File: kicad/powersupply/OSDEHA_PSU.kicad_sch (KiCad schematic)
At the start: 2 parts, among them J1 PSU HV, T1 Transformer_1P_2S

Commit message: up
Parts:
- removed T1: Transformer_1P_2S, symbol Device:Transformer_1P_2S
- added J3: AC secondaries, symbol Connector:Conn_01x06_Socket
- added R10: 976k, Resistor_THT:R_Axial_DIN0207_L6.3mm_D2.5mm_P10.16mm_Horizontal, symbol Device:R
- added R4, R9: 787k, Resistor_THT:R_Axial_DIN0207_L6.3mm_D2.5mm_P10.16mm_Horizontal, symbol Device:R
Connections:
- net HV_STABI1/AC1: now also J3.1 (Pin_1)
- net HV_STABI1/AC2: now also J3.2 (Pin_2)
- net HV_STABI2/AC1: now also J3.3 (Pin_3)
- net HV_STABI2/AC2: now also J3.4 (Pin_4)
- net HV_STABI3/DC-: now reaches J1.3 (Pin_3)
- new net HV_STABI1/RSET+: R4.2
- new net HV_STABI1/RSET-: R4.1
- new net HV_STABI2/RSET+: R9.2
- new net HV_STABI2/RSET-: R9.1
- new net HV_STABI3/AC1: J3.5 (Pin_5)
- new net HV_STABI3/AC2: J3.6 (Pin_6)
- new net HV_STABI3/RSET+: R10.2
- new net HV_STABI3/RSET-: R10.1
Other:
- added sheet HV_STABI3 (hv_stabi.kicad_sch)
- sheet HV_STABI1 ports: added RSET+, RSET-; removed none
- sheet HV_STABI2 ports: added RSET+, RSET-; removed none
- note added: "+440 V"
- note added: "-440 V"
- note added: "-550 V"
- note removed: "GRID BIAS"
- moved on the sheet: J1

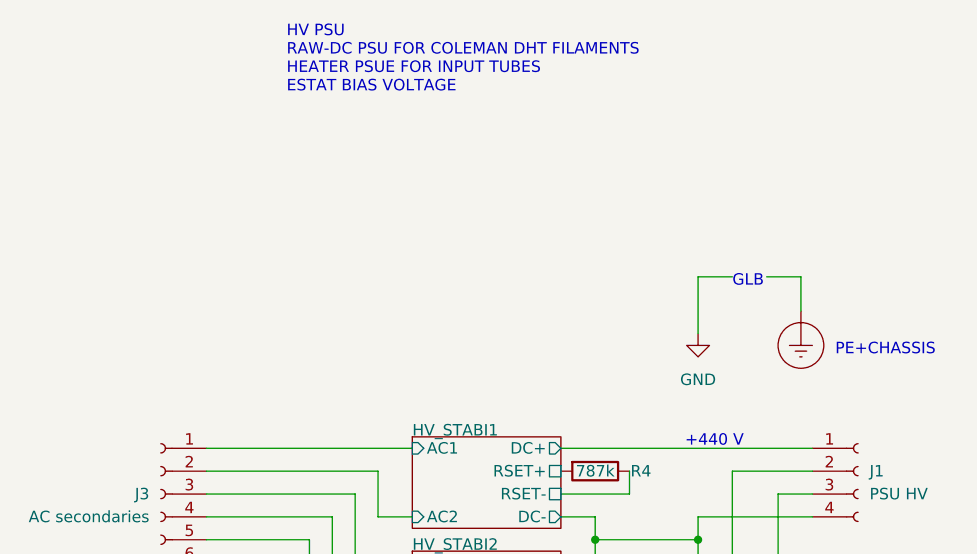
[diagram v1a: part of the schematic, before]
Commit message: add GLB
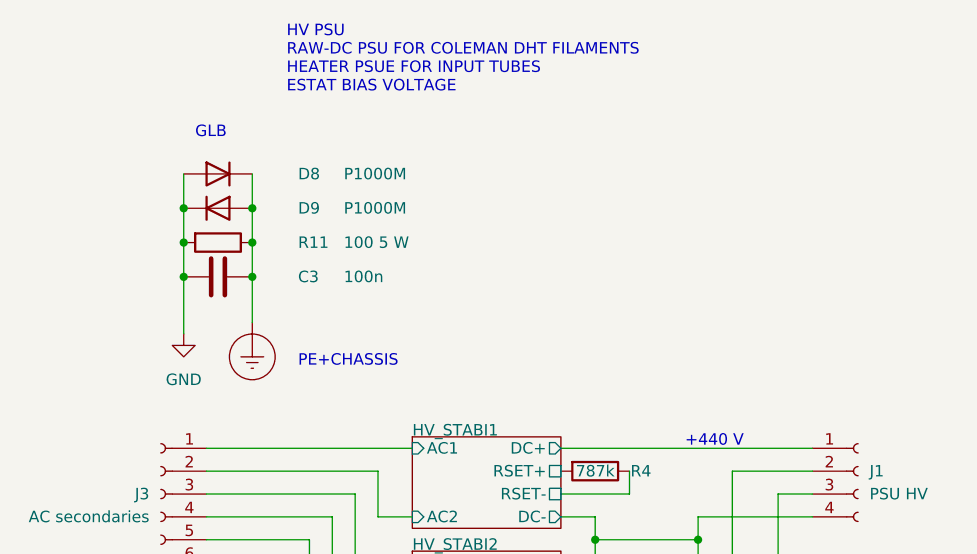
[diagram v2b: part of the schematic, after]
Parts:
- added C3: 100n, symbol Device:C
- added D8, D9: P1000M, Diode_THT:D_P600_R-6_P12.70mm_Horizontal, symbol Device:D
- added R11: 100 5 W, symbol Device:R
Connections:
- net Earth_Protective: now also C3.2, D8.1 (K), D9.2 (A), R11.1
- net GND: now also C3.1, D8.2 (A), D9.1 (K), R11.2

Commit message: up
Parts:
- added C4, C5, C6, C7: 100n 1 kV, symbol Device:C
- added D10, D11: 1N4007, Diode_THT:D_DO-41_SOD81_P10.16mm_Horizontal, symbol Diode:1N4007
- added D12, D13, D14: 150 V, symbol Device:D_Zener
- added D15: 130 V, symbol Device:D_Zener
- added Q6: 10M90S, Package_TO_SOT_THT:TO-220-3_Vertical, symbol OSDEHA_PSU:10M90S
- added R12: 3k, Resistor_THT:R_Axial_DIN0207_L6.3mm_D2.5mm_P10.16mm_Horizontal, symbol Device:R
- added R13: 15k?, Resistor_THT:R_Axial_DIN0207_L6.3mm_D2.5mm_P10.16mm_Horizontal, symbol Device:R
- added R14: 787k?, Resistor_THT:R_Axial_DIN0207_L6.3mm_D2.5mm_P10.16mm_Horizontal, symbol Device:R
- added R15, R16: 100k, Resistor_THT:R_Axial_DIN0207_L6.3mm_D2.5mm_P10.16mm_Horizontal, symbol Device:R
- added R17: 4.7M, Resistor_THT:R_Axial_DIN0207_L6.3mm_D2.5mm_P10.16mm_Horizontal, symbol Device:R
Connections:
- net GND: now also J1.2 (Pin_2), C4.2, C6.2, C7.2, D15.2 (A), R14.2; no longer J1.4 (Pin_4)
- net HV_STABI1/DC+: now also R13.2
- net HV_STABI2/DC-: now also J1.3 (Pin_3); no longer J1.2 (Pin_2)
- net HV_STABI3/AC2: now also C5.1
- net HV_STABI3/DC-: now also J1.4 (Pin_4); no longer J1.3 (Pin_3)
- new net: C5.2, D10.2 (A), D11.1 (K)
- new net: C7.1, R16.2
- new net: C4.1, D10.1 (K), Q6.2 (A+)
- new net: C6.1, R15.2
- new net: D12.1 (K), Q6.3 (K-), R12.1, R15.1, R16.1, R17.2
- new net: D12.2 (A), D13.1 (K)
- new net: Q6.1 (G), R12.2
- new net: D13.2 (A), D14.1 (K)
- new net: D14.2 (A), D15.1 (K)
- new net: D11.2 (A), R13.1, R14.1
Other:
- note added: "+440 VDC"
- note added: "-440 VDC"
- note added: "-550 VDC"
- note added: "325 VAC"
- note added: "415 VAC"
- note added: "580 VDC Bias"
- note removed: "+440 V"
- note removed: "-440 V"
- note removed: "-550 V"
- moved on the sheet: C3, D8, D9, R11

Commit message: up
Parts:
- removed D8, D9: P1000M, Diode_THT:D_P600_R-6_P12.70mm_Horizontal, symbol Device:D
- added D30: GBJ3510, Diode_THT:Diode_Bridge_32.0x5.6x17.0mm_P10.0mm_P7.5mm, symbol Diode_Bridge:B40C3x00-2200A
- added J3: PSU HV-2, Connector_Molex:Molex_KK-396_5273-04A_1x04_P3.96mm_Vertical, symbol Connector:Conn_01x04_Socket
- C2: renamed from C5; footprint (none) -> Capacitor_THT:C_Rect_L18.0mm_W9.0mm_P15.00mm_FKS3_FKP3
- C3: renamed from C4; footprint (none) -> Capacitor_THT:C_Rect_L18.0mm_W9.0mm_P15.00mm_FKS3_FKP3
- C4: renamed from C6; footprint (none) -> Capacitor_THT:C_Rect_L18.0mm_W9.0mm_P15.00mm_FKS3_FKP3
- C5: renamed from C7; footprint (none) -> Capacitor_THT:C_Rect_L18.0mm_W9.0mm_P15.00mm_FKS3_FKP3
- J2: renamed from J1; value PSU HV -> PSU HV-1
- R5: renamed from R13; value 15k? -> 47k
- R6: renamed from R14; value 787k? -> 787k
- renumbered C3 to C1, D11 to D3, D10 to D4, D12 to D5, D13 to D6, D14 to D7, D15 to D8, J3 to J1, Q6 to Q1, R11 to R1, R17 to R10, R4 to R2, R9 to R3, R10 to R4, R12 to R7, R15 to R8, R16 to R9
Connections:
- net Earth_Protective: now also D30.1 (-), D30.4 (+)
- net GND: now also D30.2, D30.3, J3.2 (Pin_2)
- net HV_STABI1/AC1: now also C2.2
- net HV_STABI1/DC+: now also J3.1 (Pin_1)
- net HV_STABI2/DC-: now also J3.3 (Pin_3)
- net HV_STABI3/AC2: no longer C2.1
- net HV_STABI3/DC-: now also J3.4 (Pin_4)
- net at D3.1 (K), D4.2 (A): now also C2.1; no longer C2.2
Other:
- note added: "GROUND-LOOP BREAKER"
- note added: "When AC swings negative: - left capacitor charge is maintained at DC supply voltage through left diode. - Max. voltage across cap = DC-(-ACpeak) = 400-(-325) = 725 V When AC swings positive: - rising AC pushes the cap charge through right diode into right cap, through the current limiter - charges the tail of the bias supply up to the Zener voltage - charge/voltage it "trapped" downstream of the 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"
- note removed: "GLB"
- moved on the sheet: C1, C2, J2, R1, R6

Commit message: up
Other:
- note added: "Filament, heater and buffer/bias supply turn on first B+ and B- turn on with delay"
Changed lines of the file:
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@@
     (effects (font (size 1.27 1.27)) (justify right bottom))
+  )
+  (text "Filament, heater and buffer/bias supply turn on first\nB+ and B- turn on with delay"
+    (at 157.48 82.55 0)
+    (effects (font (size 2.54 2.54)) (justify left bottom))
   )
   (text "325 VAC" (at 60.96 78.74 0)

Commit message: UP
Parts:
- added CHASSIS1: MountingHole_Pad, MountingHole:MountingHole_3.2mm_M3_Pad, symbol Mechanical:MountingHole_Pad
- added H1, H2, H3: MountingHole, MountingHole:MountingHole_3.2mm_M3, symbol Mechanical:MountingHole
- renumbered C2 to C1, C3 to C2, C4 to C3, C5 to C4, C1 to C5, D3 to D1, D4 to D2, D5 to D3, D6 to D4, D7 to D5, D8 to D6, D30 to D7, R2 to R1, R3 to R2, R4 to R3, R5 to R4, R6 to R5, R7 to R6, R8 to R7, R9 to R8, R1 to R9
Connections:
- net Earth_Protective: now also CHASSIS1.1

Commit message: up
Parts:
- removed J1: AC secondaries, symbol Connector:Conn_01x06_Socket
- added J4, J5: 325 VAC, TerminalBlock_Phoenix:TerminalBlock_Phoenix_MKDS-1,5-2-5.08_1x02_P5.08mm_Horizontal, symbol Connector:Screw_Terminal_01x02
- added J6: 415 VAC, TerminalBlock_Phoenix:TerminalBlock_Phoenix_MKDS-1,5-2-5.08_1x02_P5.08mm_Horizontal, symbol Connector:Screw_Terminal_01x02
- J2, J3: footprint Connector_Molex:Molex_KK-396_5273-04A_1x04_P3.96mm_Vertical -> Connector_Molex:Molex_KK-396_A-41791-0004_1x04_P3.96mm_Vertical
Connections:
- net HV_STABI1/AC1: now also J4.1 (Pin_1)
- net HV_STABI1/AC2: now also J4.2 (Pin_2)
- net HV_STABI2/AC1: now also J5.1 (Pin_1)
- net HV_STABI2/AC2: now also J5.2 (Pin_2)
- net HV_STABI3/AC1: now also J6.1 (Pin_1)
- net HV_STABI3/AC2: now also J6.2 (Pin_2)
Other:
- note removed: "325 VAC"
- note removed: "415 VAC"
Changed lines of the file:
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@@
     (stroke (width 0) (type default))
   )
-  (wire (pts (xy 68.58 83.82) (xy 74.93 83.82))
+  (wire (pts (xy 52.07 83.82) (xy 74.93 83.82))
     (stroke (width 0) (type default))
   )
@@
     (stroke (width 0) (type default))
   )
-  (wire (pts (xy 60.96 83.82) (xy 52.07 83.82))
+  (wire (pts (xy 60.96 99.06) (xy 52.07 99.06))
     (stroke (width 0) (type default))
   )
@@
     (stroke (width 0) (type default))
   )
-  (wire (pts (xy 52.07 76.2) (xy 68.58 76.2))
-    (stroke (width 0) (type default))
-  )
   (wire (pts (xy 123.19 71.12) (xy 124.46 71.12))
     (stroke (width 0) (type default))
@@
     (stroke (width 0) (type default))
   )
-  (wire (pts (xy 63.5 96.52) (xy 63.5 81.28))
-    (stroke (width 0) (type default))
-  )
   (wire (pts (xy 95.25 71.12) (xy 123.19 71.12))
     (stroke (width 0) (type default))
@@
     (stroke (width 0) (type default))
   )
-  (wire (pts (xy 63.5 81.28) (xy 52.07 81.28))
-    (stroke (width 0) (type default))
-  )
   (wire (pts (xy 262.89 106.68) (xy 262.89 120.65))
     (stroke (width 0) (type default))
@@
     (stroke (width 0) (type default))
   )
-  (wire (pts (xy 66.04 78.74) (xy 52.07 78.74))
+  (wire (pts (xy 66.04 86.36) (xy 52.07 86.36))
     (stroke (width 0) (type default))
   )
@@
     (stroke (width 0) (type default))
   )
-  (wire (pts (xy 74.93 96.52) (xy 63.5 96.52))
+  (wire (pts (xy 52.07 96.52) (xy 74.93 96.52))
     (stroke (width 0) (type default))
   )
@@
     (stroke (width 0) (type default))
   )
-  (wire (pts (xy 66.04 91.44) (xy 66.04 78.74))
+  (wire (pts (xy 66.04 91.44) (xy 66.04 86.36))
     (stroke (width 0) (type default))
   )
@@
     (stroke (width 0) (type default))
   )
-  (wire (pts (xy 60.96 104.14) (xy 60.96 83.82))
+  (wire (pts (xy 60.96 104.14) (xy 60.96 99.06))
     (stroke (width 0) (type default))
   )
@@
   )
   (wire (pts (xy 66.04 91.44) (xy 74.93 91.44))
-    (stroke (width 0) (type default))
-  )
-  (wire (pts (xy 68.58 76.2) (xy 68.58 83.82))
     (stroke (width 0) (type default))
   )
@@
     (effects (font (size 2.54 2.54)) (justify left bottom))
   )
-  (text "325 VAC" (at 60.96 78.74 0)
-    (effects (font (size 1.27 1.27)) (justify right bottom))
-  )
-  (text "325 VAC" (at 60.96 73.66 0)
-    (effects (font (size 1.27 1.27)) (justify right bottom))
-  )
   (text "-440 VDC" (at 110.49 91.44 90)
     (effects (font (size 1.27 1.27)) (justify left bottom))
   )
   (text "580 VDC Bias" (at 279.4 44.45 0)
-    (effects (font (size 1.27 1.27)) (justify right bottom))
-  )
-  (text "415 VAC" (at 60.96 83.82 0)
     (effects (font (size 1.27 1.27)) (justify right bottom))
   )
@@
     )
   )
-  (symbol (lib_id "Connector:Conn_01x06_Socket") (at 46.99 76.2 0) (mirror y) (unit 1)
-    (in_bom yes) (on_board yes) (dnp no)
-    (property "Reference" "J1" (at 45.72 76.2 0)
-      (effects (font (size 1.27 1.27)) (justify left))
-    )
-    (property "Value" "AC secondaries" (at 45.72 78.74 0)
-      (effects (font (size 1.27 1.27)) (justify left))
-    )
-    (property "Footprint" "" (at 46.99 76.2 0)
-      (effects (font (size 1.27 1.27)) hide)
-    )
-    (property "Datasheet" "~" (at 46.99 76.2 0)
-      (effects (font (size 1.27 1.27)) hide)
-    )
-    (pin "4")
-    (pin "1")
-    (pin "2")
-    (pin "3")
-    (pin "5")
-    (pin "6")
-    (instances
-      (project "OSDEHA_PSU"
-        (path "/ca37e2fa-48ac-4eb3-a7a4-1e3bbee61661"
-          (reference "J1") (unit 1)
-        )
-      )
-    )
-  )
   (symbol (lib_id "Device:C") (at 255.27 127 90) (unit 1)
     (in_bom yes) (on_board yes) (dnp no)
@@
     )
   )
+  (symbol (lib_id "Connector:Screw_Terminal_01x02") (at 46.99 83.82 0) (mirror y) (unit 1)
+    (in_bom yes) (on_board yes) (dnp no)
+    (property "Reference" "J5" (at 44.45 83.82 0)
+      (effects (font (size 1.27 1.27)) (justify left))
+    )
+    (property "Value" "325 VAC" (at 44.45 86.36 0)
+      (effects (font (size 1.27 1.27)) (justify left))
+    )
+    (property "Footprint" "TerminalBlock_Phoenix:TerminalBlock_Phoenix_MKDS-1,5-2-5.08_1x02_P5.08mm_Horizontal" (at 46.99 83.82 0)
+      (effects (font (size 1.27 1.27)) hide)
+    )
+    (property "Datasheet" "https://www.mouser.ch/ProductDetail/Phoenix-Contact/1729128?qs=sGAEpiMZZMvPvGwLNS6718PaoTt7FM7ciW3NqkEQwDE%3D" (at 46.99 83.82 0)
+      (effects (font (size 1.27 1.27)) hide)
+    )
+    (pin "2")
+    (pin "1")
+    (instances
+      (project "OSDEHA_PSU"
+        (path "/ca37e2fa-48ac-4eb3-a7a4-1e3bbee61661"
+          (reference "J5") (unit 1)
+        )
+      )
+    )
+  )
   (symbol (lib_id "Device:R") (at 252.73 46.99 0) (unit 1)
     (in_bom yes) (on_board yes) (dnp no)
@@
       (effects (font (size 1.27 1.27)) (justify left))
     )
-    (property "Footprint" "Connector_Molex:Molex_KK-396_5273-04A_1x04_P3.96mm_Vertical" (at 129.54 99.06 0)
-      (effects (font (size 1.27 1.27)) hide)
-    )
-    (property "Datasheet" "~" (at 129.54 99.06 0)
+    (property "Footprint" "Connector_Molex:Molex_KK-396_A-41791-0004_1x04_P3.96mm_Vertical" (at 129.54 99.06 0)
+      (effects (font (size 1.27 1.27)) hide)
+    )
+    (property "Datasheet" "https://www.mouser.ch/ProductDetail/Molex/41791-0851?qs=LD9zNoQ5lgUDGtVX5jMt3g%3D%3D" (at 129.54 99.06 0)
       (effects (font (size 1.27 1.27)) hide)
     )
@@
       (effects (font (size 1.27 1.27)) (justify left))
     )
-    (property "Footprint" "Connector_Molex:Molex_KK-396_5273-04A_1x04_P3.96mm_Vertical" (at 129.54 73.66 0)
-      (effects (font (size 1.27 1.27)) hide)
-    )
-    (property "Datasheet" "~" (at 129.54 73.66 0)
+    (property "Footprint" "Connector_Molex:Molex_KK-396_A-41791-0004_1x04_P3.96mm_Vertical" (at 129.54 73.66 0)
+      (effects (font (size 1.27 1.27)) hide)
+    )
+    (property "Datasheet" "https://www.mouser.ch/ProductDetail/Molex/41791-0851?qs=LD9zNoQ5lgUDGtVX5jMt3g%3D%3D" (at 129.54 73.66 0)
       (effects (font (size 1.27 1.27)) hide)
     )
@@
     )
   )
+  (symbol (lib_id "Connector:Screw_Terminal_01x02") (at 46.99 96.52 0) (mirror y) (unit 1)
+    (in_bom yes) (on_board yes) (dnp no)
+    (property "Reference" "J6" (at 44.45 96.52 0)
+      (effects (font (size 1.27 1.27)) (justify left))
+    )
+    (property "Value" "415 VAC" (at 44.45 99.06 0)
+      (effects (font (size 1.27 1.27)) (justify left))
+    )
+    (property "Footprint" "TerminalBlock_Phoenix:TerminalBlock_Phoenix_MKDS-1,5-2-5.08_1x02_P5.08mm_Horizontal" (at 46.99 96.52 0)
+      (effects (font (size 1.27 1.27)) hide)
+    )
+    (property "Datasheet" "https://www.mouser.ch/ProductDetail/Phoenix-Contact/1729128?qs=sGAEpiMZZMvPvGwLNS6718PaoTt7FM7ciW3NqkEQwDE%3D" (at 46.99 96.52 0)
+      (effects (font (size 1.27 1.27)) hide)
+    )
+    (pin "2")
+    (pin "1")
+    (instances
+      (project "OSDEHA_PSU"
+        (path "/ca37e2fa-48ac-4eb3-a7a4-1e3bbee61661"
+          (reference "J6") (unit 1)
+        )
+      )
+    )
+  )
   (symbol (lib_id "Device:R") (at 149.86 43.18 270) (unit 1)
     (in_bom yes) (on_board yes) (dnp no)
@@
         )
       )
+    )
+  )
+  (symbol (lib_id "Connector:Screw_Terminal_01x02") (at 46.99 71.12 0) (mirror y) (unit 1)
+    (in_bom yes) (on_board yes) (dnp no)
+    (property "Reference" "J4" (at 44.45 71.12 0)
+      (effects (font (size 1.27 1.27)) (justify left))
+    )
+    (property "Value" "325 VAC" (at 44.45 73.66 0)
+      (effects (font (size 1.27 1.27)) (justify left))
+    )
+    (property "Footprint" "TerminalBlock_Phoenix:TerminalBlock_Phoenix_MKDS-1,5-2-5.08_1x02_P5.08mm_Horizontal" (at 46.99 71.12 0)
+      (effects (font (size 1.27 1.27)) hide)
+    )
+    (property "Datasheet" "https://www.mouser.ch/ProductDetail/Phoenix-Contact/1729128?qs=sGAEpiMZZMvPvGwLNS6718PaoTt7FM7ciW3NqkEQwDE%3D" (at 46.99 71.12 0)
+      (effects (font (size 1.27 1.27)) hide)
+    )
+    (pin "2")
+    (pin "1")
+    (instances
+      (project "OSDEHA_PSU"
+        (path "/ca37e2fa-48ac-4eb3-a7a4-1e3bbee61661"
+          (reference "J4") (unit 1)
+        )
+      )

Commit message: up
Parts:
- added C10: 220u 600 VDC, Capacitor_THT:CP_Radial_D35.0mm_P10.00mm_SnapIn, symbol Device:C_Polarized
- added C6, C8: 470u 500 VDC, Capacitor_THT:CP_Radial_D35.0mm_P10.00mm_SnapIn, symbol Device:C_Polarized
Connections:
- net HV_STABI3/DC- is gone; now on net GND: J2.4 (Pin_4), J3.4 (Pin_4)
- new net HV_STABI1/CAP+: C6.1
- new net HV_STABI1/CAP-: C6.2
- new net HV_STABI2/CAP+: C8.1
- new net HV_STABI2/CAP-: C8.2
- new net HV_STABI3/CAP+: C10.1
- new net HV_STABI3/CAP-: C10.2
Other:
- sheet HV_STABI1 ports: added CAP+, CAP-; removed none
- sheet HV_STABI2 ports: added CAP+, CAP-; removed none
- sheet HV_STABI3 ports: added CAP+, CAP-; removed none
- note added: "B+ and B-: +/- 440 VDC, 2 x 60 mA Grid driver: -550 VDC, 2 x 20 mA"
- moved on the sheet: R3
